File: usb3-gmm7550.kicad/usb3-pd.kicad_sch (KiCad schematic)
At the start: 30 parts, among them J6 DNI, Q4 STL9P3LLH6, Q5 STL9P3LLH6, Q6 STL9P3LLH6, U18 STUSB1600, U19 LM66200DRLR

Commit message: Placement: WIP, schematic update to 0.9.1 -- BoM simplification and minor improvements
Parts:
- Q4, Q5, Q6: footprint POWERFLAT_3P3X3P3_STM -> usb3-gmm7550:POWERFLAT_3P3X3P3_STM
- U19: footprint SOT-5X3_DRL_TEX -> usb3-gmm7550:SOT-5X3_DRL_TEX
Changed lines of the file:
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@@
 	(title_block
 		(title "GMM-7550 USB3 Adapter")
-		(date "2025-07-24")
-		(rev "0.9")
+		(date "2025-08-06")
+		(rev "0.9.1")
 	)
 	(text "Copyright (c) 2025 Anton Kuzmin <ak@gmm7550.dev>\n\nThis documentation is distributed under the terms of\nthe CERN-OHL-P v2 (https://cern.ch/cern-ohl).\n\nThis project was funded through the NGI0 Common Fund,\na fund established by NLnet foundation."
@@
 	(wire
 		(pts
-			(xy 184.15 149.86) (xy 204.47 149.86)
-		)
-		(stroke
-			(width 0)
-			(type default)
-		)
-	)
-	(wire
-		(pts
 			(xy 130.81 52.07) (xy 130.81 83.82)
 		)
@@
 	(wire
 		(pts
+			(xy 187.96 152.4) (xy 204.47 152.4)
+		)
+		(stroke
+			(width 0)
+			(type default)
+		)
+	)
+	(wire
+		(pts
 			(xy 194.31 60.96) (xy 196.85 60.96)
 		)
@@
 	(wire
 		(pts
-			(xy 187.96 152.4) (xy 204.47 152.4)
-		)
-		(stroke
-			(width 0)
-			(type default)
-		)
-	)
-	(wire
-		(pts
 			(xy 88.9 107.95) (xy 88.9 116.84)
 		)
@@
 	(wire
 		(pts
+			(xy 184.15 149.86) (xy 204.47 149.86)
+		)
+		(stroke
+			(width 0)
+			(type default)
+		)
+	)
+	(wire
+		(pts
 			(xy 121.92 46.99) (xy 121.92 60.96)
 		)
@@
 			"AEEAAABBAAAAQgAAAGoAAABBAAAAQQAAAEEAAABBAAAAYwAAAGcAAABBAAAAQQAAAEEAAABHAAAA"
 			"awAAAEEAAABBAAAAQQAAAEIAAAB3AAAAQQAAAEEAAABBAAAAQQAAAGQAAABBAAAAQQAAAEEAAABB"
-			"AAAARwAAAGsAAABBAA=="
+			"AAAARwAAAGsAAABBAEFBQUFBQUFBQUFBQUFBQWdBQUtRQUFBQUFBQUFBY0FRQUFIQUVBQUFBQUFB"
+			"QVZBZ0FBT3dBQUFOTUNBQUFMQUFBQTB3SUFBQXdBQUFBQUFBQUFxMVlBQUxBTkpLbXJWZ0FBTUE0"
+			"a3FhdFdBQUIwYUhKbGMyaHZiR1FBQUFBQUFBQUFBQUlBQUJRQkFBRHdEU1NwcTFZQUFBQUFBQUEw"
+			"QUFBQTB3SUFBQXdBQUFEVEFnQUFGUUFBQUFBQUFBQ3JWZ0FBQUE0a3FhdFdBQUJ3RGlTcHExWUFB"
+			"QUJOUVVFY0FRQUFIQUVBQUFBQUFBQkZURjlUU1ZwRkFOTUNBQUFWQUFBQTB3SUFBQllBQUFBQUFB"
+			"QUFxMVlBQUVBT0pLbXJWZ0FBc0E0a3FhdFdBQUFBQWdBQVBRQUFBRDBBQUFBQUFBQUFXUUlBQUJR"
+			"QUFBRFRBZ0FBRmdBQUFOTUNBQUFYQUFBQUFBQUFBS3RXQUFDQURpU3BxMVlBQVBBT0pLbXJWZ0FB"
+			"QUE0a3FSd0JBQUFjQVFBQUFBQUFBRGhXajZtclZnQUEwd0lBQUJjQUFBRFRBZ0FBR0FBQUFBQUFB"
+			"QUNyVmdBQXdBNGtxYXRXQUFEb0VTU3BxMVlBQUdac2IyRjBNZ0FBQUE4a3FSUUJBQUFBRHlTcHEx"
+			"WUFBQUFHSktrVUFRQUEwd0lBQUJnQUFBRFRBZ0FBSGdBQUFBQUFBQUF0QUFBQUNBOGtxYXRXQUFC"
+			"NER5U3BxMVlBQUFBUEpLa29BQUFBS0FBQUFBQUFBQUJBVjQrcHExWUFBTk1DQUFBZUFBQUEwd0lB"
+			"QUI4QUFBQUFBQUFBcTFZQUFFZ1BKS21yVmdBQVlCSWtxYXRXQUFCVFRVRkJYMVJJVWtWVFNFOU1S"
+			"QUFBQUJRa3FSUUJBQUNJRHlTcHExWUFBRGdISkttclZnQUEwd0lBQUI4QUFBRFRBZ0FBTFFBQUFB"
+			"QUFBQUE2QUFBQW1BOGtxYXRXQUFBSUVHOVZZbFJ3WlU1UFJFOUtiMHhuWlU5UVFtcHRSalZEU1ZO"
+			"QlVXbEhiVVJLU0M5QlFrTkJXSHBrTW5KNVZWSkthVEZqTDNRMVVsSkRjR2RyZWpGRGNIQjRaSE5P"
+			"VmpOeVJVVmFNR1V6Tm5oUlpqWktTamxTWVU1MmVuQk5kbHB3VlRBM2NGVXdTMjF3VUc1WGQwbE5O"
+			"RXRGTUV0alZuaE5ZM2RQZUVWeGNWTnJibEV6YTIxdE1ETkVVVzlwWVRBclRYSnRjRkZwYmxsbFVW"
+			"WlplbFpHYTB4alVqRjNWVWhqWlZsVlltaHRaR2RvYjFCMlIwaEViV1ZOWnpaQmJIRlVaRFJpWjFk"
+			"UFMyRm9TVEJ0VTJaUwAAAAAAAAAAAAAAAAAAAADwBQAAAAAAAEAAAAAAAAAAHq+8EWhZAABtAAAA"
+			"LgAAAEUAAABuAAAAYQAAAGIAAABsAAAAZQAAAAAAAAAAAAAAYO5kh21ZAADhBAAAAAAAAEAdUoVt"
+			"WQAAsN5kh21ZAAAAAAAAAAAAAAAAAAAAAAAAUOhkh21ZAAALAAAAAAAAAAsAAAAAAAAARwAAAE4A"
+			"AAAAAAAAAAAAAAAAAAAAAAAAkOhkh21ZAAAkAAAAAAAAACQAAAAAAAAACAAAAAAAAAAAAAAAAAAA"
+			"AAAAAAAAAAAAAAAAAAAAAAAxBAAAAAAAAKDCZIdtWQAAIOsv8Wh1AAAAAAAAAAAAAAAAAAAAAAAA"
+			"IAAAAGYAAABpAAAAZQAAAGwAAABkAAAAIAAAAHcAAABhAAAAcgAAAG4AAABpAAAAbgAAAGcAAAAg"
+			"AAAAcwAAAHkAAABtAAAAYgAAAG8AAABsAAAALAAAACAAAABsAAAAYQAAAHIAAABnAAAAZQAAAKAA"
+			"AAAAAAAAkAMAAAAAAAAA6GSHbVkAABAAAAAAAAAAEAAAAAAAAAAAAAAAAAAAAAAAAAAAAAAAAAAA"
+			"AAAAAAAIAAAAAQAAAADqZIdtWQAABgAAAAAAAAAGAAAAAAAAAAAAAAAAAAAAAAAAAAAAAAAAAAAA"
+			"AAAAAAQAAAABAAAAMOpkh21ZAAAEAAAAAAAAAAQAAAAAAAAAAAAAAAAAAAAAAAAAAAAAAAAAAAAA"
+			"AAAABAAAAAFZAABQ6mSHbVkAAAgAAAAAAAAACAAAAAAAAAAAAAAAAAAAAAAAAAAAAAAAAAAAAAAA"
+			"AAAEAAAAAQAAAIDqZIdtWQAABQAAAAAAAAAFAAAAAAAAALAAAAAAAAAAAAAAAAAAAAAAAAAAAAAA"
+			"AAQAAAABWQAAoOpkh21ZAAAHAAAAAAAAAAcAAAAAAAAAAQAAAAAAAAAAAAAAAAAAAAAAAAAAAAAA"
+			"BAAAAAEAAAAQ8WSHbVkAAAEAAAAAAAAAfgAAAAAAAAAAAAAAAAAAAAAAAAAAAAAAAAAAAAAAAAAE"
+			"AAAAAVkAABDvZIdtWQAAJAAAAAAAAAAkAAAAAAAAAGAGAAAAAAAAAAAAAAAAAAAAAAAAAAAAAAQA"
+			"AAABAAAAgPFkh21ZAAAAAAAAAAAAAAAAAAAAAAAAAAAAAAAAAAAAAAAAAAAAAAAAAAAAAAAABAAA"
+			"AAEAAABA82SHbVkAAAQAAAAAAAAABAAAAAAAAAAAAAAAAAAAAAAAAAAAAAAAAAAAAAAAAAAEAAAA"
+			"AVkAAPDxZIdtWQAAAQAAAAAAAAAwAAAAAAAAAGAom3ttWQAAAAAAAAAAAAAAAAAAAAAAAAQAAAAB"
+			"WQAAYPNkh21ZAAAQAA=="
 		)
 	)
@@
 			"AAAAAAAAAAAAAAAAAAAAAAAAAAAAAAAAAAAAAAAAAAAAAAAAAAAAAAAAAAAAAAAAAAAAAAAAAAAA"
 			"AAAAAAAAAAAAAAAAAAAAAAAAAAAAAAAAAAAAAAAAAAAAAAAAAAAAAAAAAAAAAAAAAAAAAAAAAAAA"
-			"AAAAAAAAAAAAAAAAAAAAAA=="
+			"AAAAAAAAAAAAAAAAAAAAAAAAAAAAAAAAAAAAAAAAAAAAAAAAAAAAAAAAAAAAAAAAAAAAAAAAAAAA"
+			"AAAAAAAAAAAAAAAAAAAAAAAAAAAAAAAAAAAAAAAAAAAAAAAAAAAAAAAAAAAAAAAAAAAAAAAAAAAA"
+			"AAAAAAAAAAAAAAAAAAAAAAAAAAAAAAAAAAAAAAAAAAAAAAAAAAAAAAAAAAAAAAAAAAAAAAAAAAAA"
+			"AAAAAAAAAAAAAAAAAAAAAAAAAAAAAAAAAAAAAAAAAAAAAAAAAAAAAAAAAAAAAAAAAAAAAAAAAAAA"
+			"AAAAAAAAAAAAAAAAAAAAAAAAAAAAAAAAAAAAAAAAAAAAAAAAAAAAAAAAAAAAAAAAAAAAAAAAAAAA"
+			"AAAAAAAAAAAAAAAAAAAAAAAAAAAAAAAAAAAAAAAAAAAAAAAAAAAAAAAAAAAAAAAAAAAAAAAAAAAA"
+			"AAAAAAAAAAAAAAAAAAAAAAAAAAAAAAAAAAAAAAAAAAAAAAAAAAAAAAAAAAAAAAAAAAAAAAAAAAAA"
+			"AAAAAAAAAAAAAAAAAAAAAAAAAAAAAAAAAAAAAAAAAAAAAAAAAAAAAAAAAAAAAAAAAAAAAAAAAAAA"
+			"AAAAAAAAAAAAAAAAAAAAAAAAAAAAAAAAAAAAAAAAAAAAAAAAAAAAAAAAAAAAAAAAAAAAAAAAAAAA"
+			"AAAAAAAAAAAAAAAAAAAAAAAAAAAAAAAAAAAAAAAAAAAAAAAAAAAAAAAAAAAAAAAAAAAAAAAAAAAA"
+			"AAAAAAAAAAAAAAAAAAAAAAAAAAAAAAAAAAAAAAAAAAAAAAAAAAAAAAAAAAAAAAAAAAAAAAAAAAAA"
+			"AAAAAAAAAAAAAAAAAAAAAAAAAAAAAAAAAAAAAAAAAAAAAAAAAAAAAAAAAAAAAAAAAAAAAAAAAAAA"
+			"AAAAAAAAAAAAAAAAAAAAAAAAAAAAAAAAAAAAAAAAAAAAAAAAAAAAAAAAAAAAAAAAAAAAAAAAAAAA"
+			"AAAAAAAAAAAAAAAAAAAAAAAAAAAAAAAAAAAAAAAAAAAAAAAAAAAAAAAAAAAAAAAAAAAAAAAAAAAA"
+			"AAAAAAAAAAAAAAAAAAAAAAAAAAAAAAAAAAAAAAAAAAAAAAAAAAAAAAAAAAAAAAAAAAAAAAAAAAAA"
+			"AAAAAAAAAAAAAAAAAAAAAAAAAAAAAAAAAAAAAAAAAAAAAAAAAAAAAAAAAAAAAAAAAAAAAAAAAAAA"
+			"AAAAAAAAAAAAAAAAAAAAAAAAAAAAAAAAAAAAAAAAAAAAAAAAAAAAAAAAAAAAAAAAAAAAAAAAAAAA"
+			"AAAAAAAAAAAAAAAAAAAAAAAAAAAAAAAAAAAAAAAAAAAAAAAAAAAAAAAAAAAAAAAAAAAAAAAAAAAA"
+			"AAAAAAAAAAAAAAAAAAAAAAAAAAAAAAAAAAAAAAACAAAAAAAAAAAAAAAAAAAAAgAAAAAAAAAAAAAA"
+			"AAAAAAEAAAAAAAAAAAAAAAAAAAAAAAAAAAAAAAAAAAAAAAAAAAAAAAAAAAAAAAAAAAAAAAAAAAAA"
+			"AAAAAAAAAAAAAAAAAAAAAAAAAAAAAAAAAAAAAAAAAAAAAAAAAAAAAAAAAAIAAAAAAAAAAAAAAAAA"
+			"AAACAAAAAAAAAAAAAAAAAAAAAQAAAAAAAAAAAAAAAAAAAAAAAAAAAAAAAAAAAAAAAAAAAAAAAAAA"
+			"AAAAAAAAAAAAAAAAAAAAAAAAAAAAAAAAAAAAAAAAAAAAAAAAAAAAAAAAAAAAAAAAAAAAAAAAAAAA"
+			"AgAAAAAAAAAAAAAAAAAAAAIAAAAAAAAAAAAAAAAAAAABAAAAAAAAAAAAAAAAAAAAAAAAAAAAAAAA"
+			"AAAAAAAAAAAAAAAAAAAAAAAAAAAAAAAAAAAAAAAAAAAAAAAAAAAAAAAAAAAAAAAAAAAAAAAAAAAA"
+			"AAAAAAAAAAAAAAAAAAACAAAAAAAAAAAAAAAAAAAAAgAAAAAAAAAAAAAAAAAAAAEAAAAAAAAAAAAA"
+			"AAAAAAAAAAAAAAAAAAAAAAAAAAAAAAAAAAAAAAAAAAAAAAAAAAAAAAAAAAAAAAAAAAAAAAAAAAAA"
+			"AAAAAAAAAAAAAAAAAAAAAAAAAAAAAAAAAAAAAAIAAAAAAAAAAAAAAAAAAAACAAAAAAAAAAAAAAAA"
+			"AAAAAQAAAAAAAAAAAAAAAAAAAAAAAAAAAAAAAAAAAAAAAAAAAAAAAAAAAAAAAAAAAAAAAAAAAAAA"
+			"AAAAAAAAAAAAAAAAAAAAAAAAAAAAAAAAAAAAAAAAAAAAAAAAAAAAAAAAAQAAAAAAAAAAAAAAAAAA"
+			"AAEAAAAAAAAAAAAAAAAAAAABAAAAAAAAAAAAAAAAAAAAAAAAAAAAAAAAAAAAAAAAAAAAAAAAAAAA"
+			"AAAAAAAAAAAAAAAAAAAAAAAAAAAAAAAAAAAAAAAAAAAAAAAAAAAAAAAAAAAAAAAAAAAAAAAAAAAA"
+			"AAAAAAAAAAAAAAAAAAAAAAAAAAAAAAAAAAAAAAAAAAAAAAAAAAAAAAAAAAAAAAAAAAAAAAAAAAAA"
+			"AAAAAAAAAAAAAAAAAAAAAAAAAAAAAAAAAAAAAAAAAAAAAAAAAAAAAAAAAAAAAAAAAAAAAAAAAAAA"
+			"AAAAAAAAAAAAAAAAACAAAAAyAAAAMAAAAFYAAAAgAAAAZAAAAFEHAAAAAAAAkGyfh21ZAACg1Ax4"
+			"bVkAAAAAAAAAAAAAAAAAAAAAAABhAAAAYgAAAGkAAABsAAAAaQAAAHQAAAB5AAAALAAAACAAAAAz"
+			"AAAALgAAADAAAAAuAAAALg=="
 		)
 	)
@@
 			)
 		)
-		(property "Footprint" "POWERFLAT_3P3X3P3_STM"
+		(property "Footprint" "usb3-gmm7550:POWERFLAT_3P3X3P3_STM"
 			(at 147.32 49.53 0)
 			(effects
@@
 			)
 		)
-		(property "Footprint" "POWERFLAT_3P3X3P3_STM"
+		(property "Footprint" "usb3-gmm7550:POWERFLAT_3P3X3P3_STM"
 			(at 147.32 88.9 0)
 			(effects
@@
 			)
 		)
-		(property "Footprint" "SOT-5X3_DRL_TEX"
+		(property "Footprint" "usb3-gmm7550:SOT-5X3_DRL_TEX"
 			(at 196.85 46.99 0)
 			(effects
@@
 			)
 		)
-		(property "Footprint" "POWERFLAT_3P3X3P3_STM"
+		(property "Footprint" "usb3-gmm7550:POWERFLAT_3P3X3P3_STM"
 			(at 196.85 88.9 0)
 			(effects

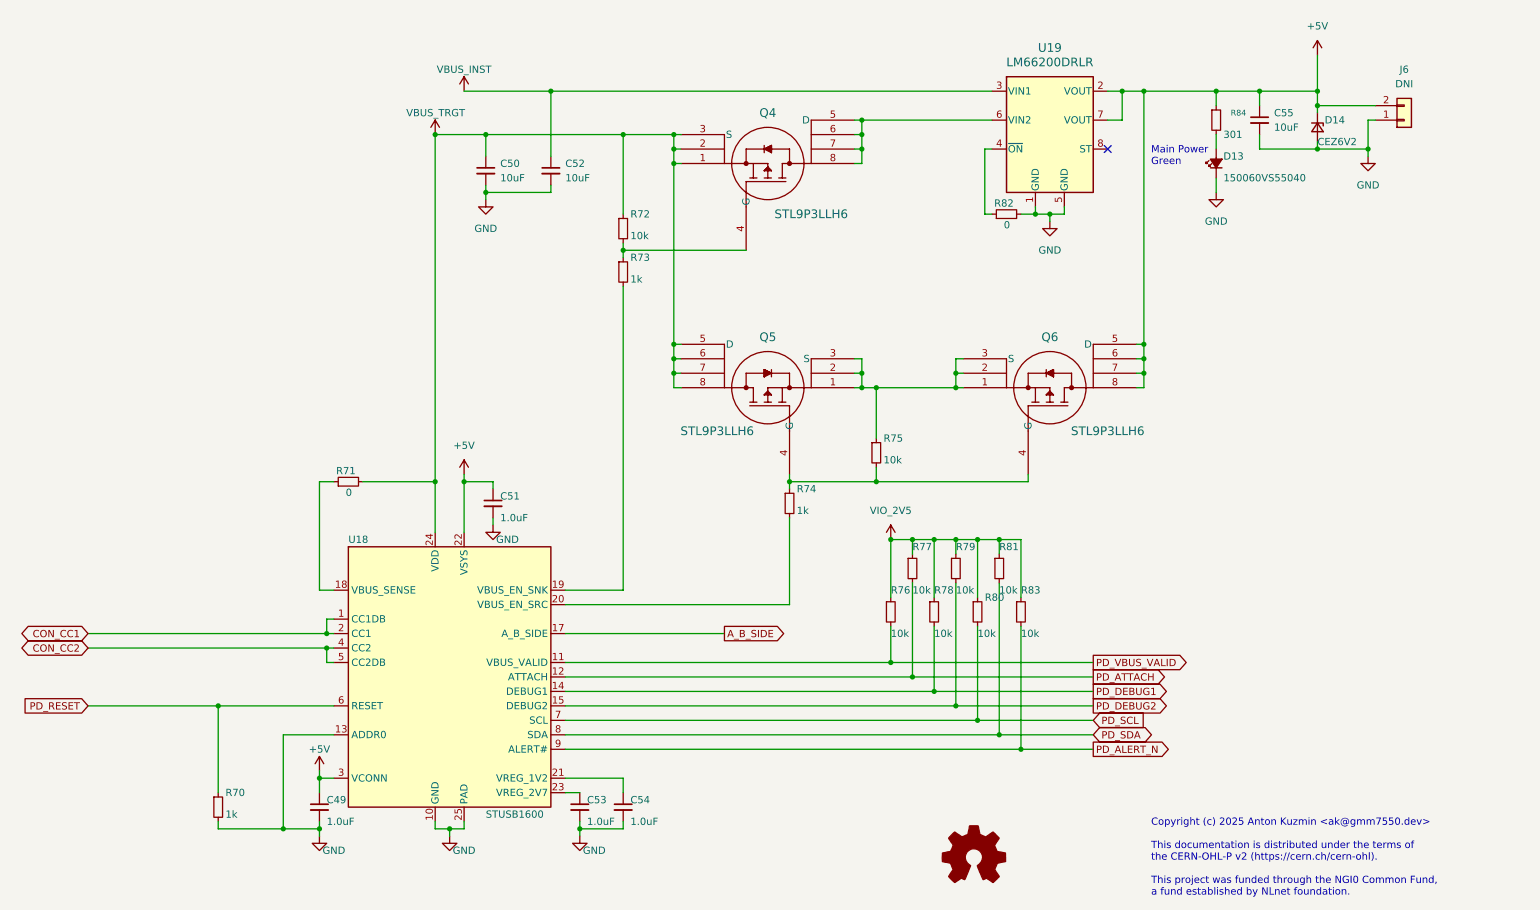
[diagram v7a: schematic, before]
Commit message: USB Power Delivery redesign (STmicro controller is NRND)
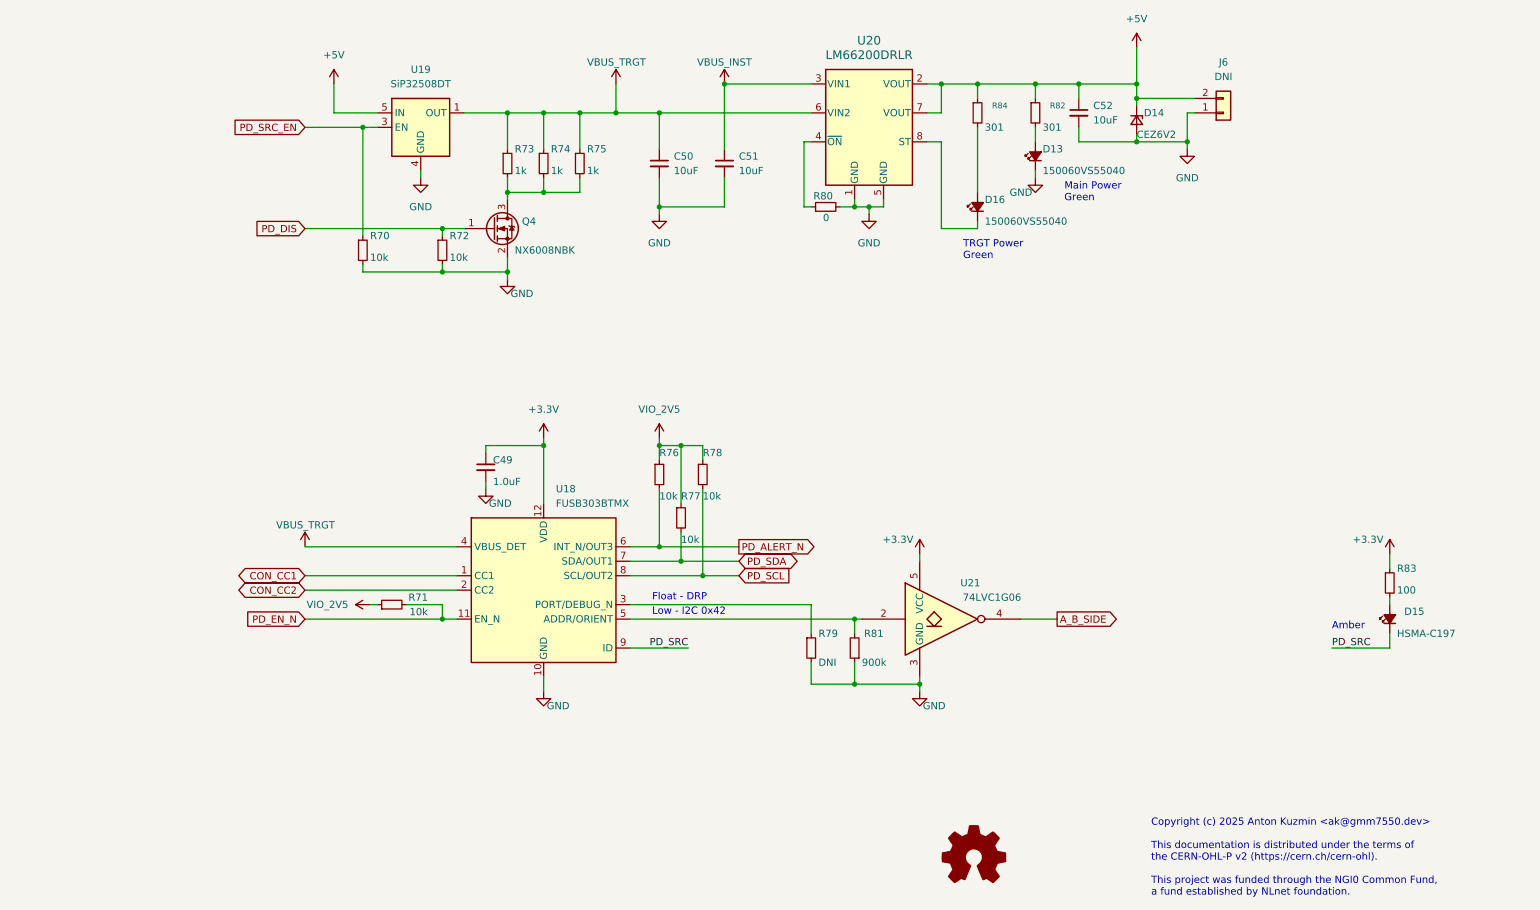
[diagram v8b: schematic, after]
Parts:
- removed C49, C51, C54: 1.0uF, Capacitor_SMD:C_0402_1005Metric, symbol Device:C_Small
- removed Q4, Q5, Q6: STL9P3LLH6, usb3-gmm7550:POWERFLAT_3P3X3P3_STM, symbol usb3-gmm7550:STL9P3LLH6
- removed R80, R81: 10k, Resistor_SMD:R_0402_1005Metric, symbol Device:R_Small
- removed U18: STUSB1600, Package_DFN_QFN:QFN-24-1EP_4x4mm_P0.5mm_EP2.7x2.7mm_ThermalVias, symbol usb3-gmm7550:STUSB1600
- added D15: HSMA-C197, LED_SMD:LED_0603_1608Metric, symbol Device:LED_Small_Filled
- added D16: 150060VS55040, LED_SMD:LED_0603_1608Metric, symbol Device:LED_Small_Filled
- added Q4: NX6008NBK, Package_TO_SOT_SMD:SOT-23, symbol Device:Q_NMOS_GSD
- added R75: 1k, Resistor_SMD:R_0402_1005Metric, symbol Device:R_Small
- added R84: 301, Resistor_SMD:R_0402_1005Metric, symbol Device:R_Small
- added U18: FUSB303BTMX, usb3-gmm7550:OnSemi_X2QFN-12_1.6x1.6mm, symbol usb3-gmm7550:FUSB303B
- added U19: SiP32508DT, Package_TO_SOT_SMD:TSOT-23-6, symbol Power_Management:SiP32508DT
- added U21: 74LVC1G06, Package_TO_SOT_SMD:SOT-23-5, symbol 74xGxx:74LVC1G06
- R79: renamed from R70; value 1k -> DNI
- R81: renamed from R71; value 0 -> 900k
- R83: value 10k -> 100
- renumbered C53 to C49, C52 to C51, C55 to C52, R72 to R70, R76 to R71, R75 to R72, R77 to R76, R78 to R77, R79 to R78, R82 to R80, R84 to R82, U19 to U20
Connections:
- net PD_ATTACH is gone; now on net PD_ALERT_N: R76.2
- net PD_DEBUG1 is gone; now on net PD_SDA: R77.2
- net PD_DEBUG2 is gone; now on net PD_SCL: R78.2
- net +5V: now also R84.1, U19.5 (IN), U19.6 (IN)
- net A_B_SIDE: now also U21.4
- net CON_CC1: now also U18.1 (CC1)
- net CON_CC2: now also U18.2 (CC2)
- net GND: now also R70.2, R72.2, R81.1, Q4.2 (S), U18.10 (GND), U19.4 (GND), U21.3 (GND)
- net PD_ALERT_N: now also U18.6 (INT_N/OUT3); no longer R83.2
- net PD_SCL: now also U18.8 (SCL/OUT2)
- net PD_SDA: now also U18.7 (SDA/OUT1)
- net VBUS_TRGT: now also R73.1, R74.1, U20.6 (VIN2), R75.1, U18.4 (VBUS_DET), U19.1 (OUT), U19.2 (OUT); no longer R70.1, R81.2
- net VIO_2V5: no longer R83.1
- net at R73.2: now also R74.2, Q4.3 (D), R75.2
- net PD_DIS: now reaches R72.1
- net PD_DIS: now also Q4.1 (G)
- net +3.3V: now reaches C49.1
- net +3.3V: now also R83.1, U18.12 (VDD), U21.5 (VCC)
- net at U20.8 (ST): now also D16.1 (K)
- net PD_RESET: no longer names the net of R79.1
- net PD_RESET: now also U18.3 (PORT/DEBUG_N)
- net PD_VBUS_VALID renamed PD_EN_N
- net PD_EN_N: now also U18.11 (EN_N)
- new net: R81.2, U18.5 (ADDR/ORIENT), U21.2
- new net: D15.2 (A), R83.2
- new net: D16.2 (A), R84.2
- new net PD_SRC: D15.1 (K), U18.9 (ID)
- new net PD_SRC_EN: R70.1, U19.3 (EN)
- no-connect marks 1 -> 0
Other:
- note added: "Amber"
- note added: "Float - DRP"
- note added: "Low - I2C 0x42"
- note added: "TRGT Power Green"
- moved on the sheet: C49, C50, C51, C52, D13, D14, J6, R70, R71, R72, R73, R74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
